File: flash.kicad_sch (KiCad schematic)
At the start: 13 parts, among them U10 IS25LP128F-JBLE

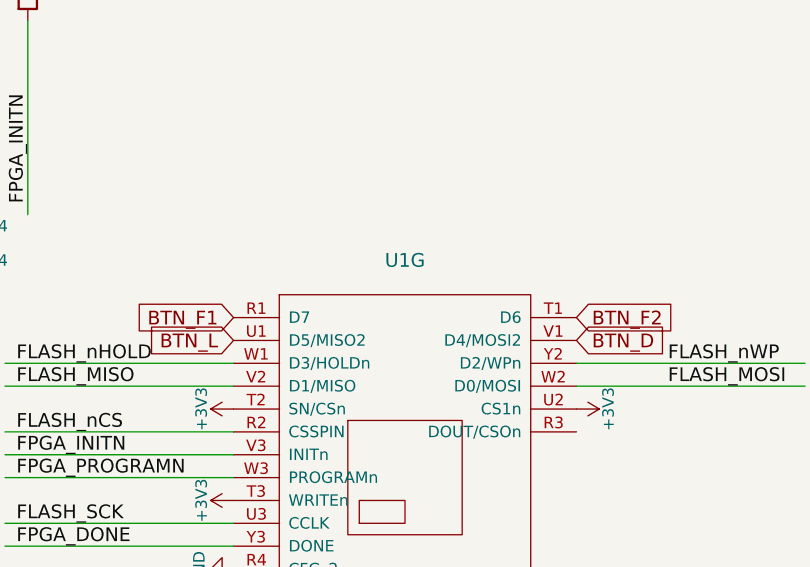
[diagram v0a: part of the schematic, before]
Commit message: Adding USB-C
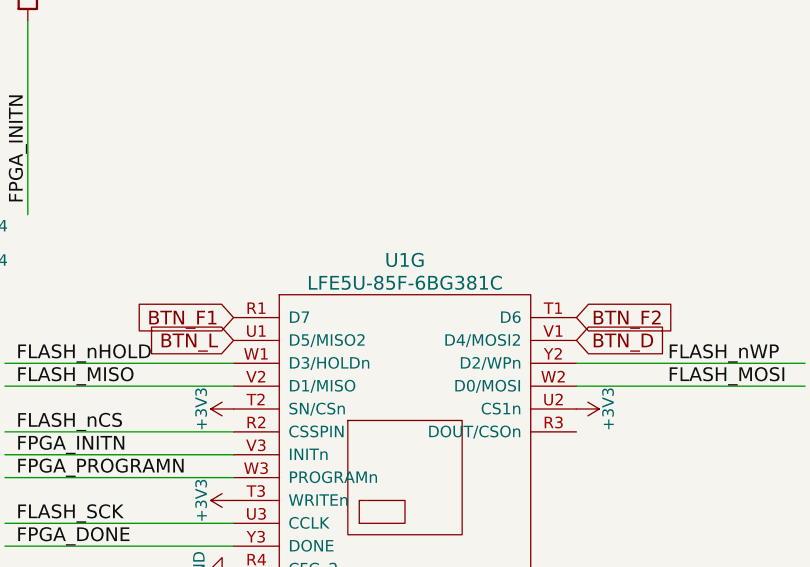
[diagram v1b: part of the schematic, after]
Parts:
- U1: value (none) -> LFE5U-85F-6BG381C; footprint (none) -> lfe5bg381:BGA-381_pitch0.8mm_dia0.4mm
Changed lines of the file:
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@@
   (title_block
     (title "ULX3S")
-    (rev "1.0.6")
+    (date "2023-01-19")
+    (rev "3.1.8")
     (company "EMARD")
     (comment 1 "SPI flash")
@@
       (effects (font (size 1.524 1.524)))
     )
-    (property "Value" "" (id 1) (at 184.15 92.71 0)
+    (property "Value" "LFE5U-85F-6BG381C" (id 1) (at 184.15 92.71 0)
       (effects (font (size 1.524 1.524)))
     )
-    (property "Footprint" "" (id 2) (at 157.48 90.17 0)
+    (property "Footprint" "lfe5bg381:BGA-381_pitch0.8mm_dia0.4mm" (id 2) (at 157.48 90.17 0)
       (effects (font (size 1.524 1.524)) hide)
     )
